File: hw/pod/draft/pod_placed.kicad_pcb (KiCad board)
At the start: 4 copper layers, 20 x 10 mm, 52 parts, among them J1 TestPoint_Pad_D1.0mm, J2 TestPoint_Pad_D1.0mm, J3 TestPoint_Pad_D1.0mm, J4 TestPoint_Pad_D1.0mm, J5 TestPoint_Pad_D1.0mm, J6 TestPoint_Pad_D1.0mm, Q1 SOT1216_L1.1-W1.0-P0.35-BL-EP, Q2 SOT1216_L1.1-W1.0-P0.35-BL-EP, SW1 SW-SMD_L3.0-W2.0-LS3.5, U1 QFN-48-1EP_7x7mm_P0.5mm_EP5.6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, U2 Knowles_LGA-5_3.5x2.65mm, U3 SOT-23-5, U4 X2SON-4_L1.0-W1.0-P0.65-TL-EP, Y1 FC-135R_L3.2-W1.5

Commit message: Draft route run 2: 0 DRC errors, 8 connections unrouted; render script; 150-pass rerun in progress
Co-Authored-By: Claude Opus 5.5 <noreply@anthropic.com>
Claude-Session: https://claude.ai/code/session_016uLR3rVesNK6FmgR7vwByF
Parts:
- moved R1 1.12 mm to (15.8, 0.80)
- moved L1 0.60 mm to (17.4, 8.60)
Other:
- outline, holes or cut-outs redrawn

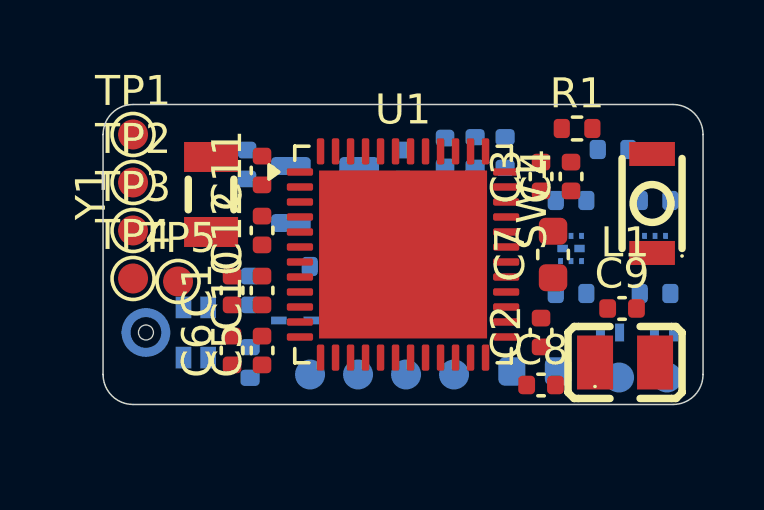
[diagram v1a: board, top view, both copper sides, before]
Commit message: Pod board 20x11.5 mm (was 10): the QFN's escape was starved; still fits the pod (12.4 mm inner)
Co-Authored-By: Claude Opus 5.5 <noreply@anthropic.com>
Claude-Session: https://claude.ai/code/session_016uLR3rVesNK6FmgR7vwByF
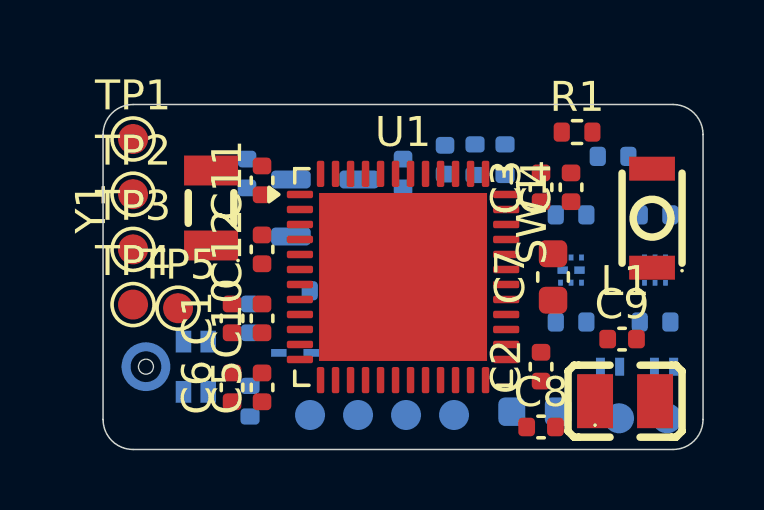
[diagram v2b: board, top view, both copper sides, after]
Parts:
- moved C8 1.40 mm to (14.6, 10.8)
- moved J1 1.36 mm to (17.2, 10.5)
- moved J2 1.36 mm to (18.8, 10.5)
- moved J3 1.35 mm to (6.90, 10.3)
- moved J4 1.35 mm to (8.50, 10.3)
- moved J5 1.35 mm to (10.1, 10.3)
- moved J6 1.35 mm to (11.7, 10.3)
- moved C14 1.34 mm to (14.4, 10.2)
- moved L1 1.29 mm to (17.4, 9.89)
- moved R2 1.29 mm to (4.90, 9.89)
- moved C5 1.23 mm to (5.30, 9.43)
- moved C6 1.23 mm to (4.30, 9.43)
- moved C2 1.14 mm to (14.6, 8.74)
- moved D1 1.14 mm to (16.9, 8.74)
- moved D2 1.14 mm to (18.7, 8.74)
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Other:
- board size 20 x 10 mm -> 20 x 11.5 mm
